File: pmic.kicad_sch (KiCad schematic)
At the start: 60 parts, among them J501 EMI shield frame, U501 STPMIC1DPQR

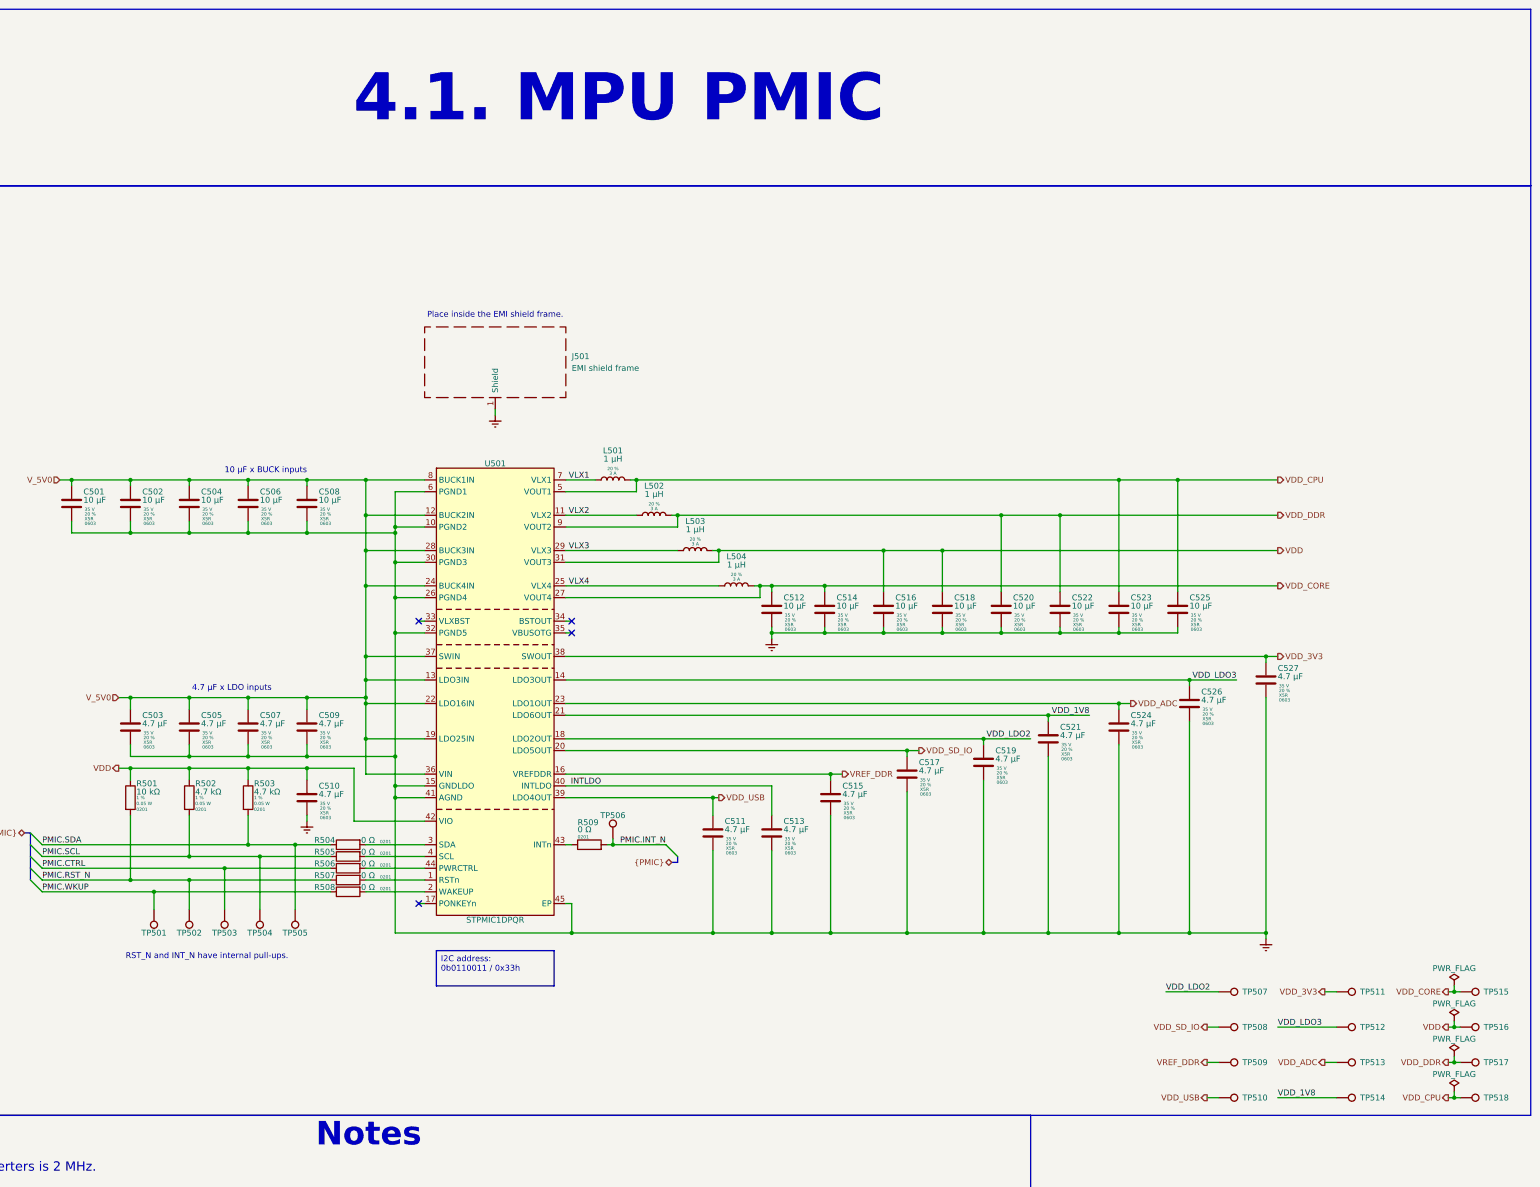
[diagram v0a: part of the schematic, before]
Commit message: Rework the schematics
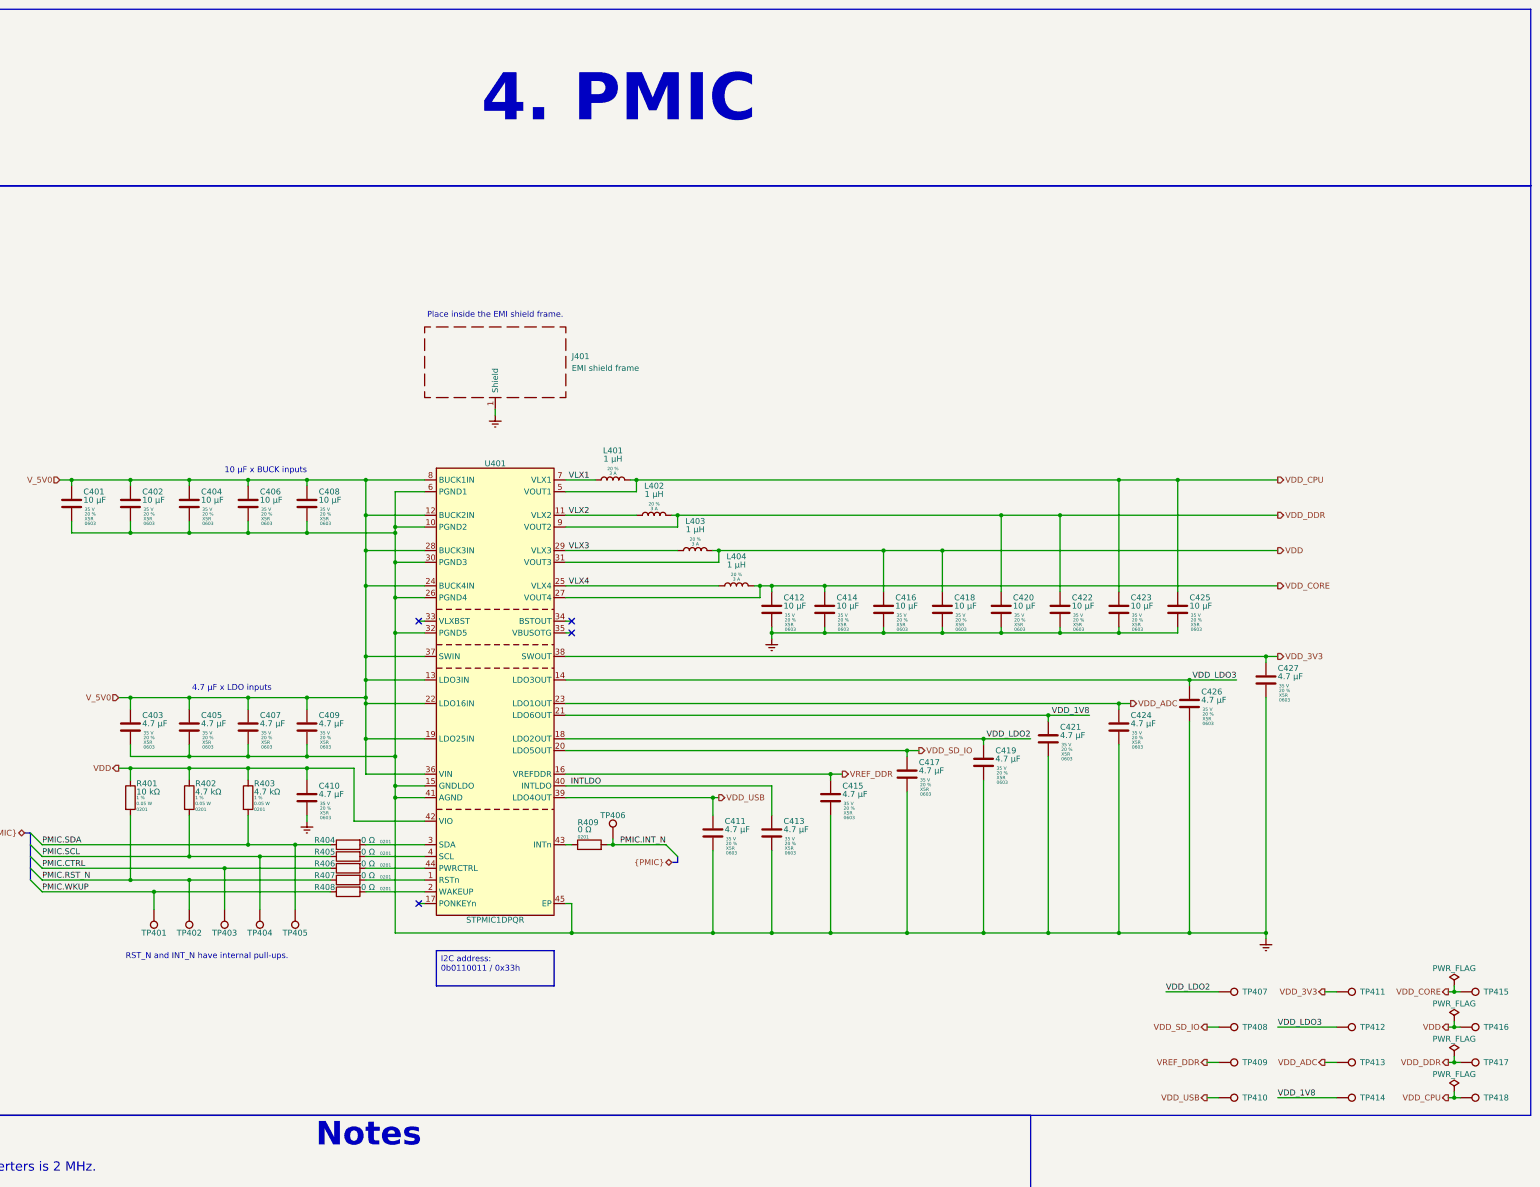
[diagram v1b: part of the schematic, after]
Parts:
- renumbered C501 to C401, C502 to C402, C503 to C403, C504 to C404, C505 to C405, C506 to C406, C507 to C407, C508 to C408, C509 to C409, C510 to C410, C511 to C411, C512 to C412, C513 to C413, C514 to C414, C515 to C415, C516 to C416, C517 to C417, C518 to C418, C519 to C419, C520 to C420, C521 to C421, C522 to C422, C523 to C423, C524 to C424, C525 to C425, C526 to C426, C527 to C427, J501 to J401, L501 to L401, L502 to L402, L503 to L403, L504 to L404, R501 to R401, R502 to R402, R503 to R403, R504 to R404, R505 to R405, R506 to R406, R507 to R407, R508 to R408, R509 to R409, TP501 to TP401, TP502 to TP402, TP503 to TP403, TP504 to TP404, TP505 to TP405, TP506 to TP406, TP507 to TP407, TP508 to TP408, TP509 to TP409, TP510 to TP410, TP511 to TP411, TP512 to TP412, TP513 to TP413, TP514 to TP414, TP515 to TP415, TP516 to TP416, TP517 to TP417, TP518 to TP418, U501 to U401

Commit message: Rework text boxes
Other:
- note added: "Notes"
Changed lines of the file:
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@@
 		(members "PMIC.SDA" "PMIC.SCL" "PMIC.CTRL" "PMIC.RST_N" "PMIC.WKUP" "PMIC.INT_N")
+	)
+	(rectangle
+		(start 12.7 50.8)
+		(end 406.4 251.46)
+		(stroke
+			(width 0)
+			(type default)
+		)
+		(fill
+			(type none)
+		)
+	)
+	(rectangle
+		(start 12.7 251.46)
+		(end 298.45 284.48)
+		(stroke
+			(width 0)
+			(type default)
+		)
+		(fill
+			(type none)
+		)
 	)
 	(text "RST_N and INT_N have internal pull-ups."
@@
 		)
 	)
+	(text "Notes"
+		(exclude_from_sim no)
+		(at 13.97 254 0)
+		(effects
+			(font
+				(size 5.08 5.08)
+				(thickness 1.016)
+				(bold yes)
+			)
+			(justify left top)
+		)
+	)
 	(text "10 µF x BUCK inputs"
 		(exclude_from_sim no)
@@
 				(size 1.27 1.27)
 			)
-		)
-	)
-	(text_box "Notes"
-		(exclude_from_sim no)
-		(at 12.7 251.46 0)
-		(size 285.75 33.02)
-		(margins 0.9525 2 0.9525 0.9525)
-		(stroke
-			(width 0)
-			(type solid)
-		)
-		(fill
-			(type none)
-		)
-		(effects
-			(font
-				(size 5.08 5.08)
-				(thickness 1.016)
-				(bold yes)
-			)
-			(justify top)
 		)
 	)
@@
 		)
 	)
-	(text_box ""
-		(exclude_from_sim no)
-		(at 12.7 50.8 0)
-		(size 393.7 200.66)
-		(margins 0.9525 2 0.9525 0.9525)
-		(stroke
-			(width 0)
-			(type solid)
-		)
-		(fill
-			(type none)
-		)
-		(effects
-			(font
-				(size 5.08 5.08)
-				(thickness 1.016)
-				(bold yes)
-			)
-			(justify top)
-		)
-	)

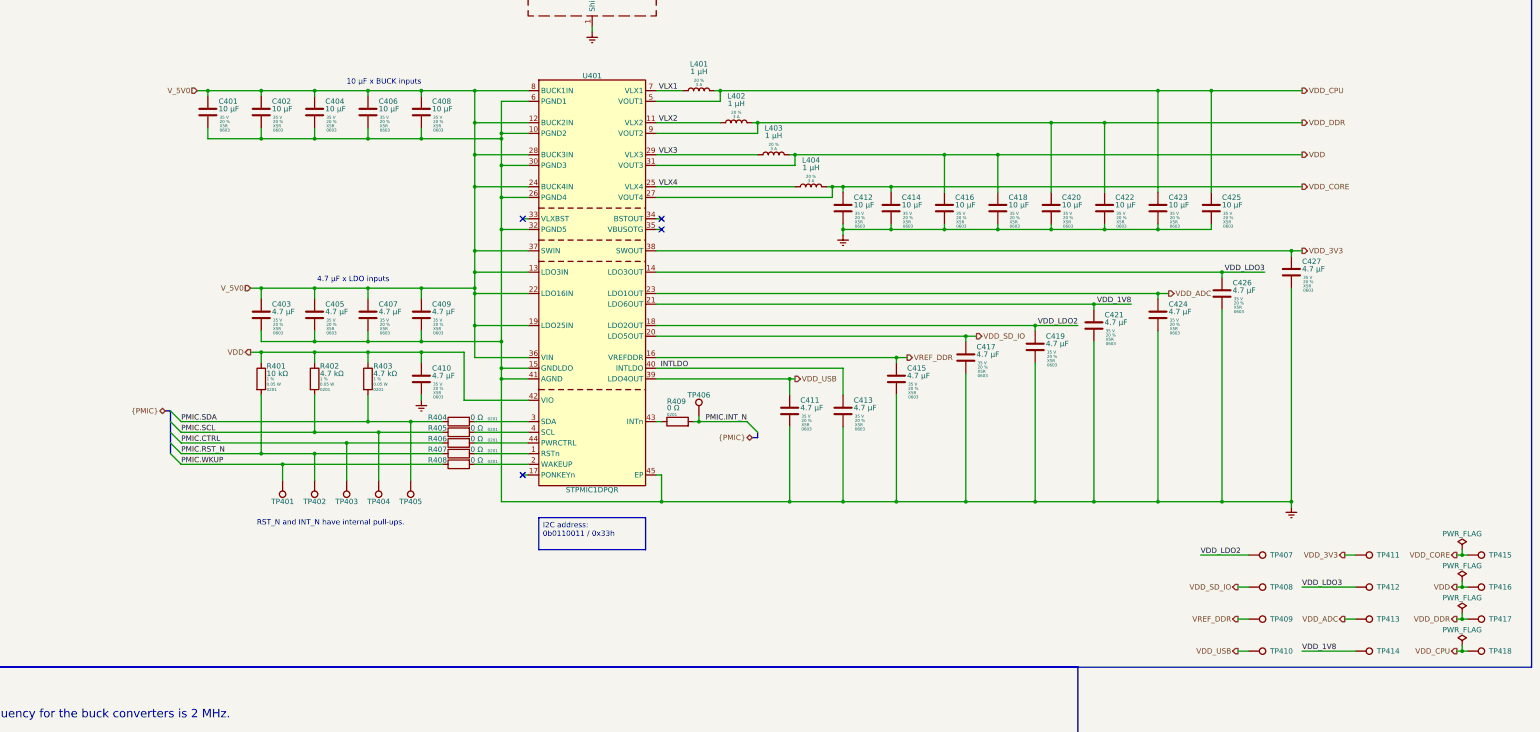
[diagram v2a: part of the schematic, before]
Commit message: Fix PMIC symbol and MPU labels
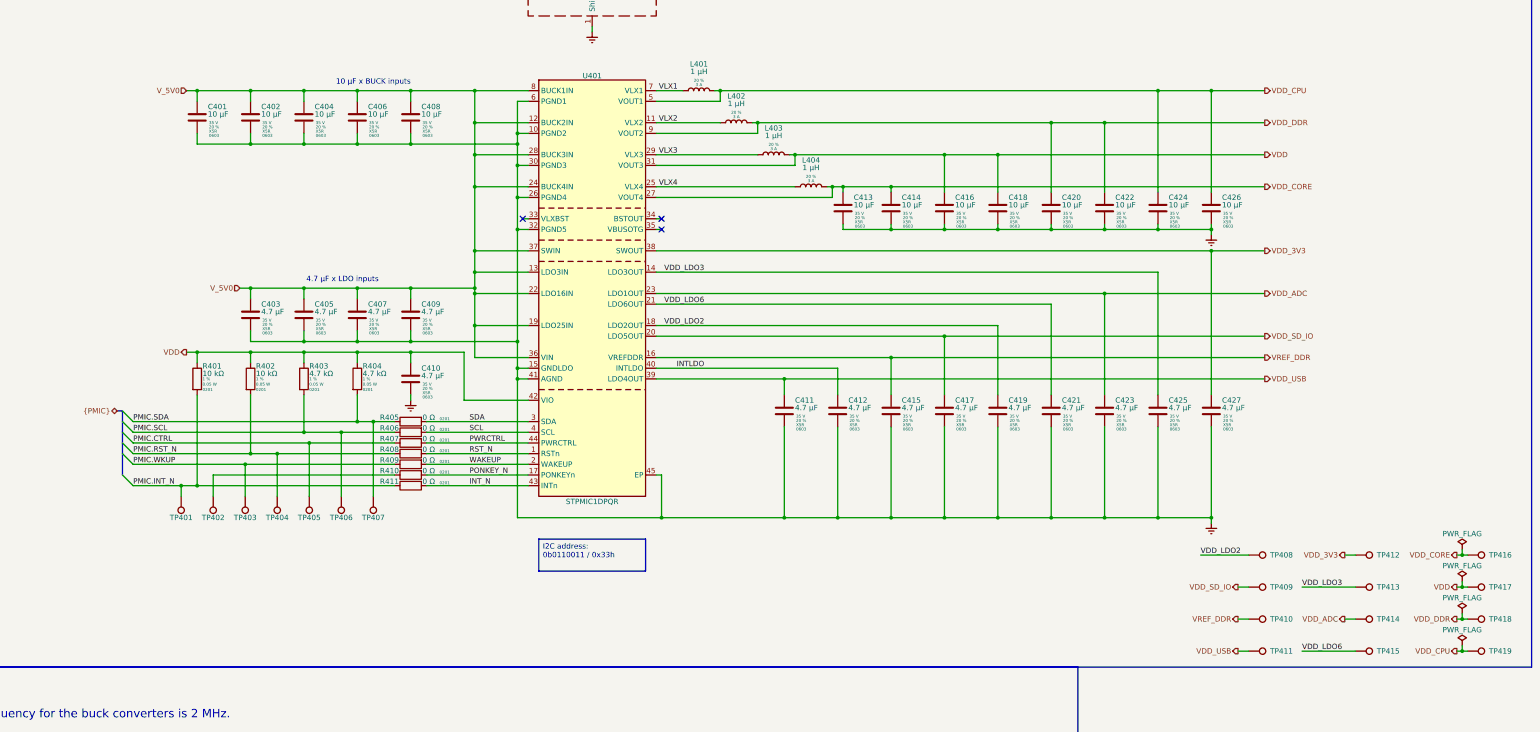
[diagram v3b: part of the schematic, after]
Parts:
- removed R409: 0 Ω, perfect_footprints:R_0201_0603Metric, symbol Device:R
- removed TP406: TestPoint, TestPoint:TestPoint_Pad_D1.0mm, symbol Connector:TestPoint
- added R401: 10 kΩ, perfect_footprints:R_0201_0603Metric, symbol Device:R
- added R410, R411: 0 Ω, perfect_footprints:R_0201_0603Metric, symbol Device:R
- added TP401, TP402: TestPoint, TestPoint:TestPoint_Pad_D1.0mm, symbol Connector:TestPoint
- renumbered C413 to C412, C412 to C413, C424 to C423, C423 to C424, C426 to C425, C425 to C426, R401 to R402, R402 to R403, R403 to R404, R404 to R405, R405 to R406, R406 to R407, R407 to R408, R408 to R409, TP401 to TP403, TP402 to TP404, TP403 to TP405, TP404 to TP406, TP405 to TP407, TP407 to TP408, TP408 to TP409, TP409 to TP410, TP410 to TP411, TP411 to TP412, TP412 to TP413, TP413 to TP414, TP414 to TP415, TP415 to TP416, TP416 to TP417, TP417 to TP418, TP418 to TP419
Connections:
- net PMIC.INT_N: now also R401.2, R411.1, TP401.1
- net VDD: now also R401.1
- net RST_N: now reaches R408.2, U401.1 (RSTn)
- net PONKEY_N: now reaches U401.17 (PONKEYn)
- net PONKEY_N: now also R410.2
- net WAKEUP: now reaches R409.2, U401.2 (WAKEUP)
- net SDA: now reaches R405.2, U401.3 (SDA)
- net SCL: now reaches R406.2, U401.4 (SCL)
- net INT_N: now reaches U401.43 (INTn)
- net INT_N: now also R411.2
- net PWRCTRL: now reaches R407.2, U401.44 (PWRCTRL)
- net VDD_1V8 renamed VDD_LDO6
- new net: R410.1, TP402.1
- no-connect marks 4 -> 3
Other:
- note removed: "RST_N and INT_N have internal pull-ups."
- moved on the sheet: C401, C402, C403, C404, C405, C406, C407, C408, C409, C410, C411, C412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

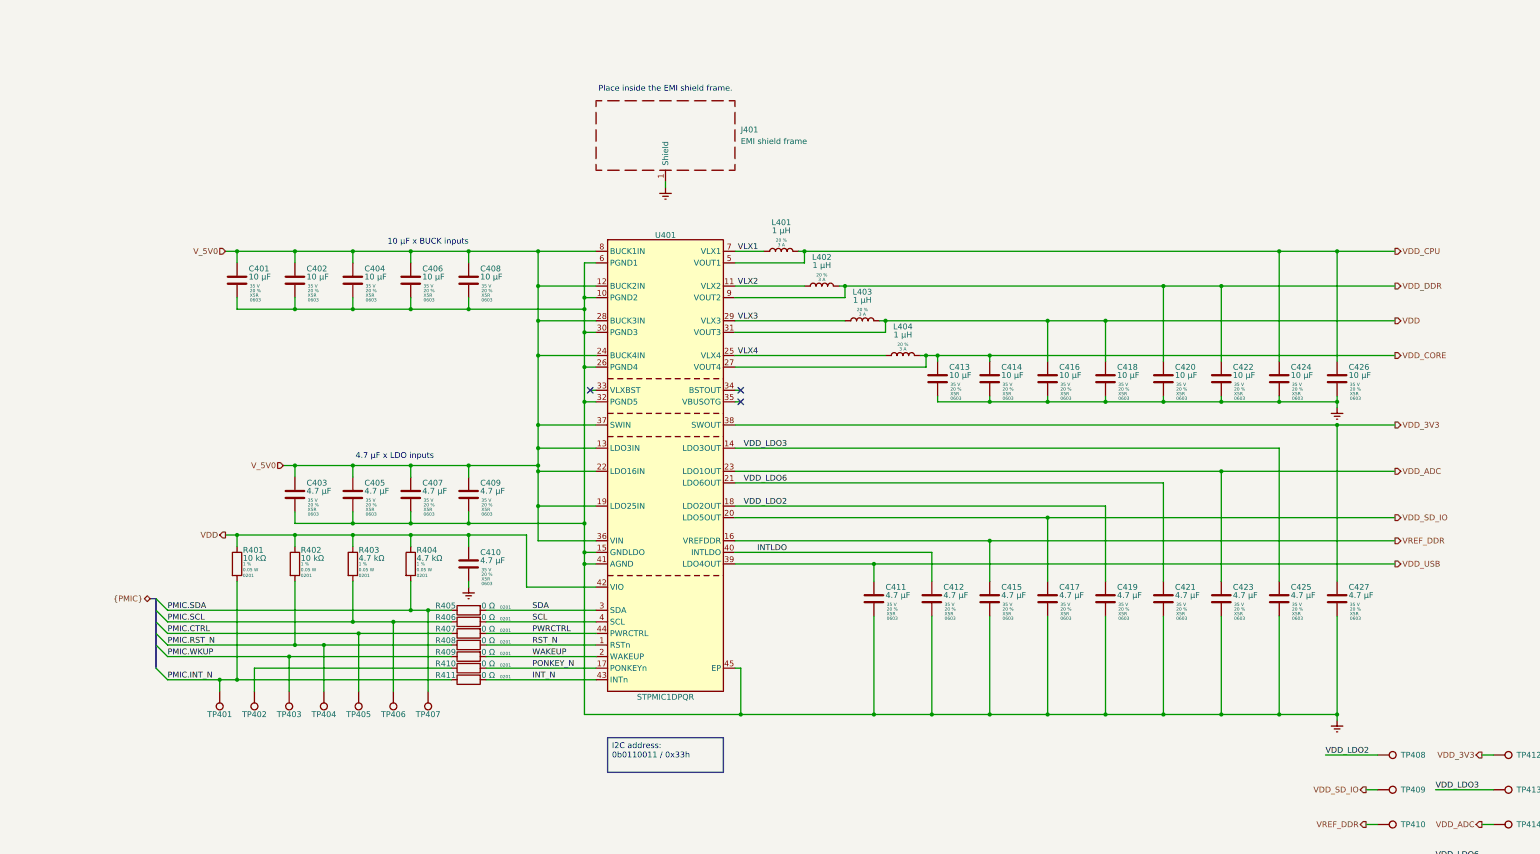
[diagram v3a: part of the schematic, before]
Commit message: Refactor PMIC
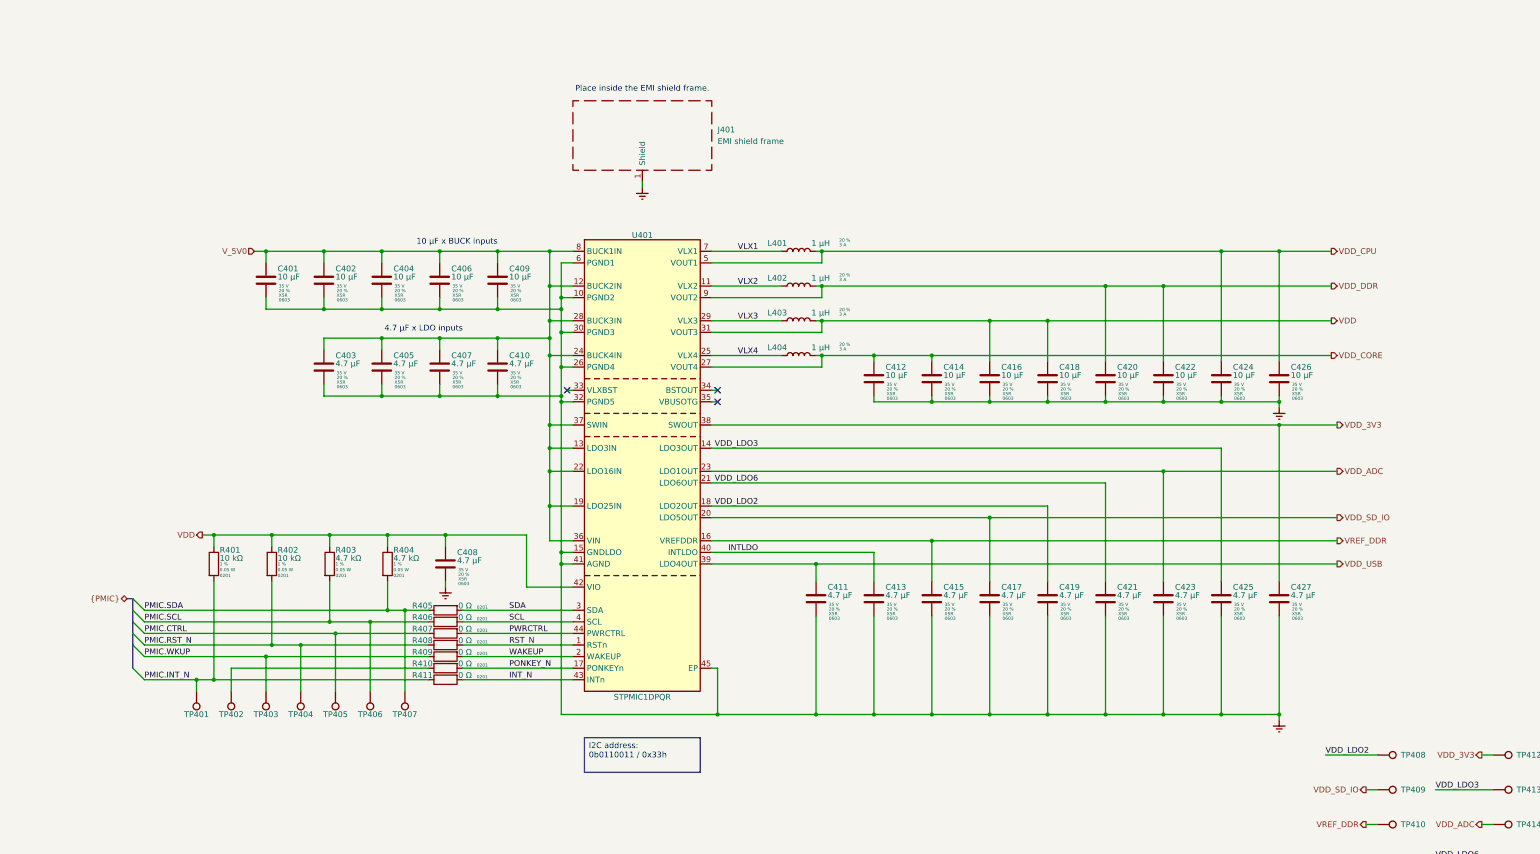
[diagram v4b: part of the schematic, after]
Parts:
- renumbered C410 to C408, C408 to C409, C409 to C410, C413 to C412, C412 to C413
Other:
- moved on the sheet: C401, C402, C403, C404, C405, C406, C407, C408, C409, C410, C411, C412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
